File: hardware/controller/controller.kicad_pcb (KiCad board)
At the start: 4 copper layers, 59 x 47 mm, 55 parts, among them J1 Conn_01x02_Pin, J11 Barrel_Jack, J12 USB_C_Receptacle_USB2.0_14P, J2 Conn_01x02_Pin, J3 Conn_01x02_Pin, J5 Screw_Terminal_01x02, J6 Screw_Terminal_01x02, J7 Conn_01x04_Pin, J8 Conn_01x04_Pin, U1 ESP32-C3-MINI-1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

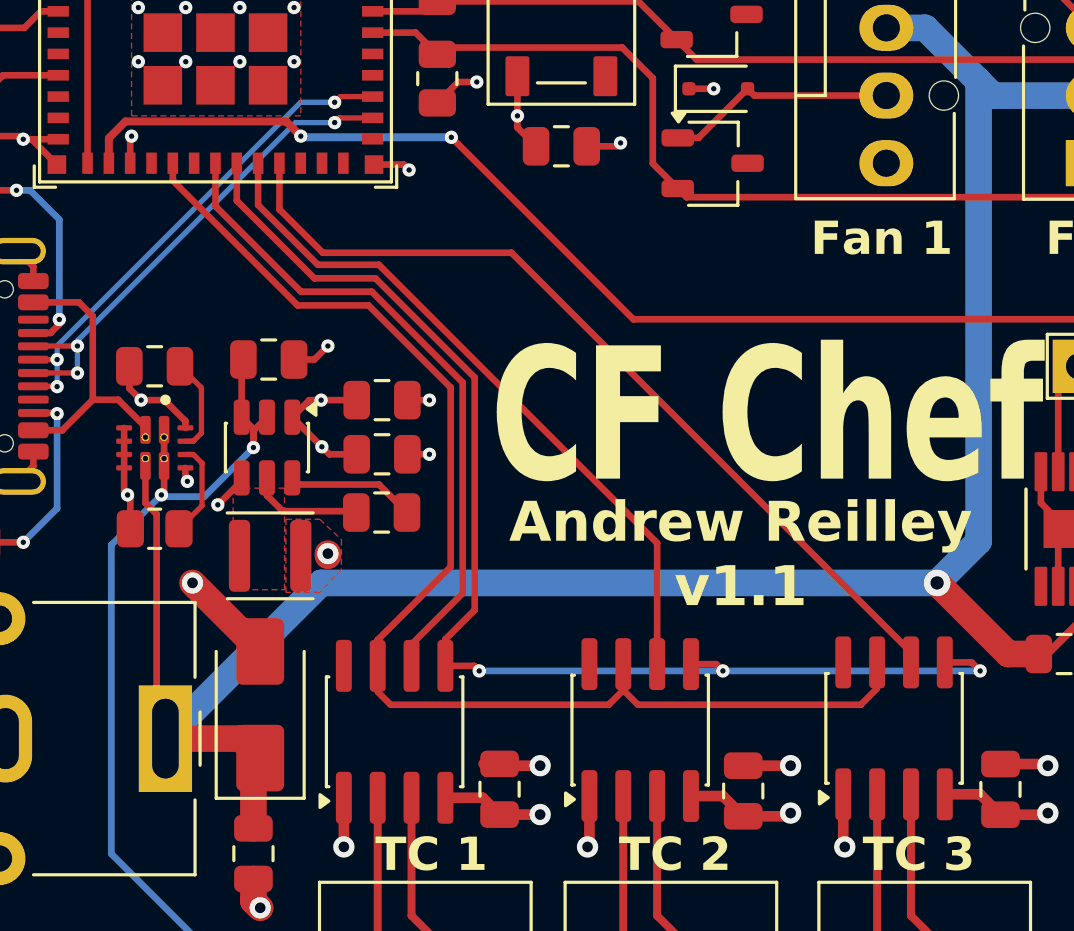
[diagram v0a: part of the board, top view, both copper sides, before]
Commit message: Reroute regulator
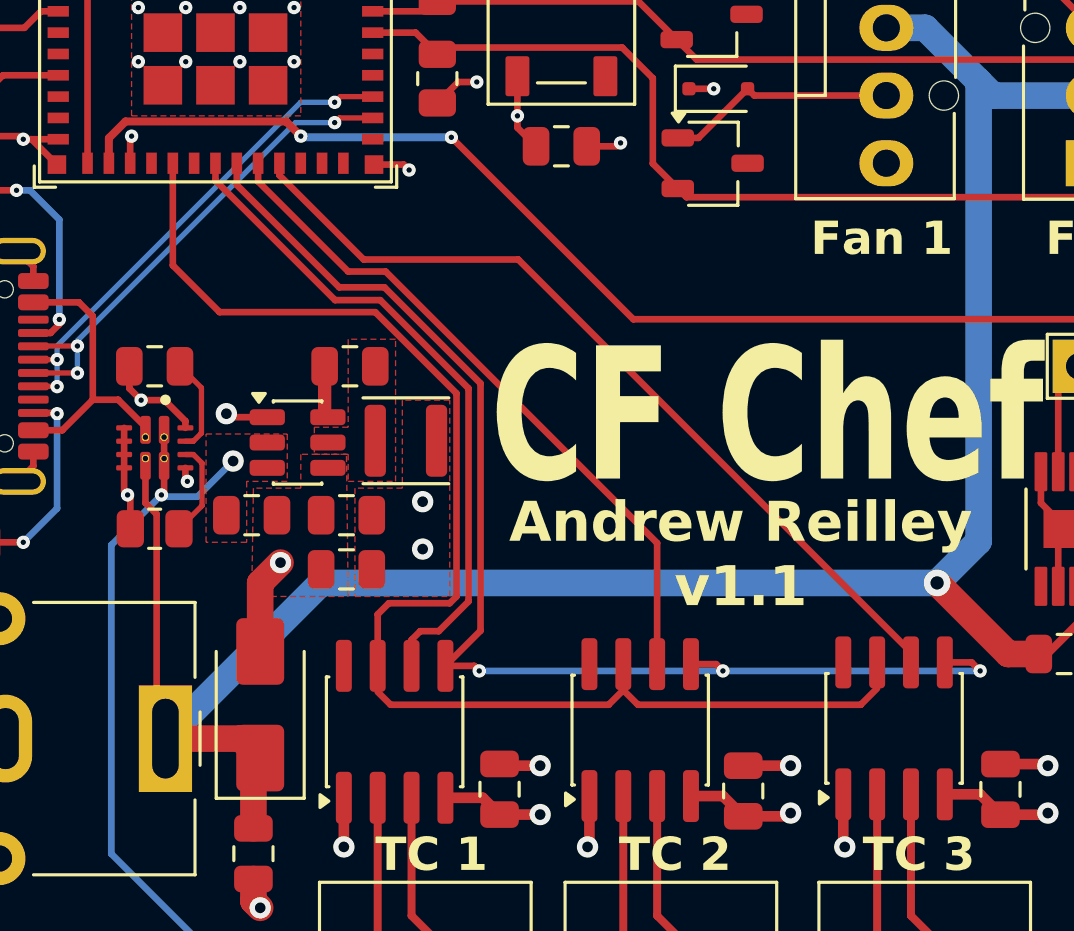
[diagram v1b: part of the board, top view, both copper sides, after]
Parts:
- moved L1 6.68 mm to (128.7, 93.0)
- moved C10 6.49 mm to (126.4, 97.8), turned to 180 degrees
- moved C11 5.88 mm to (122.9, 95.8)
- moved C13 5.61 mm to (126.6, 90.2), turned to 180 degrees
- moved C9 2.65 mm to (126.4, 95.8), turned to 180 degrees
- moved U8 1.16 mm to (124.6, 93.0), turned to 0 degrees
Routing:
- net VBUS: track 32.0 -> 26.2 mm
- net GND: track 78.7 -> 74.1 mm, vias 48 -> 44
- net Net-(U8-SW): track 4.28 -> 0.00 mm
- net +3V3: track 28.5 -> 24.3 mm
- net SO: track 45.5 -> 48.9 mm
- net Net-(U8-BST): track 4.84 -> 2.13 mm
- net CS2: track 32.7 -> 31.9 mm
- net CS1: track 26.3 -> 25.8 mm
- added copper zone on F.Cu, net VBUS

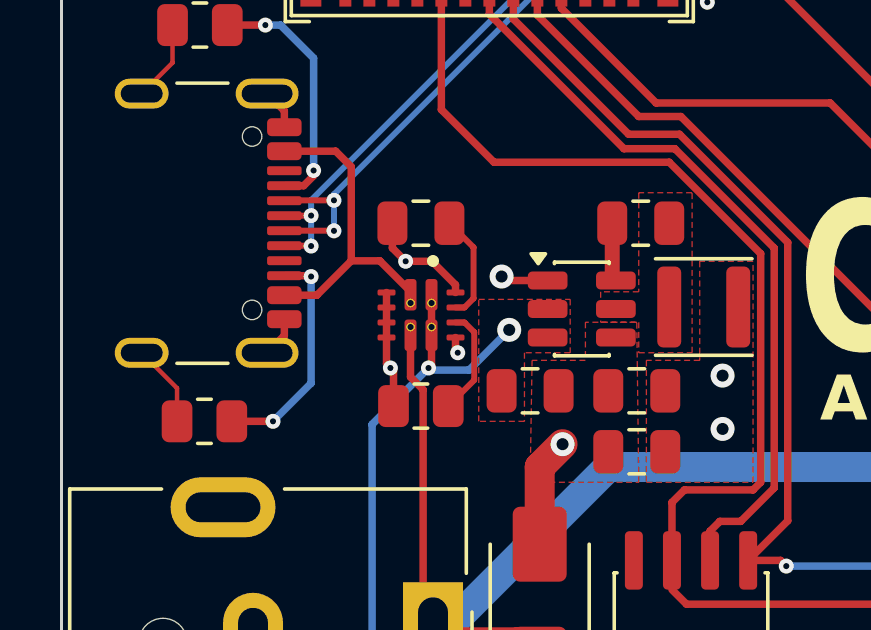
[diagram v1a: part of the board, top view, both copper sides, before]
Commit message: Increase via size for manufacturing
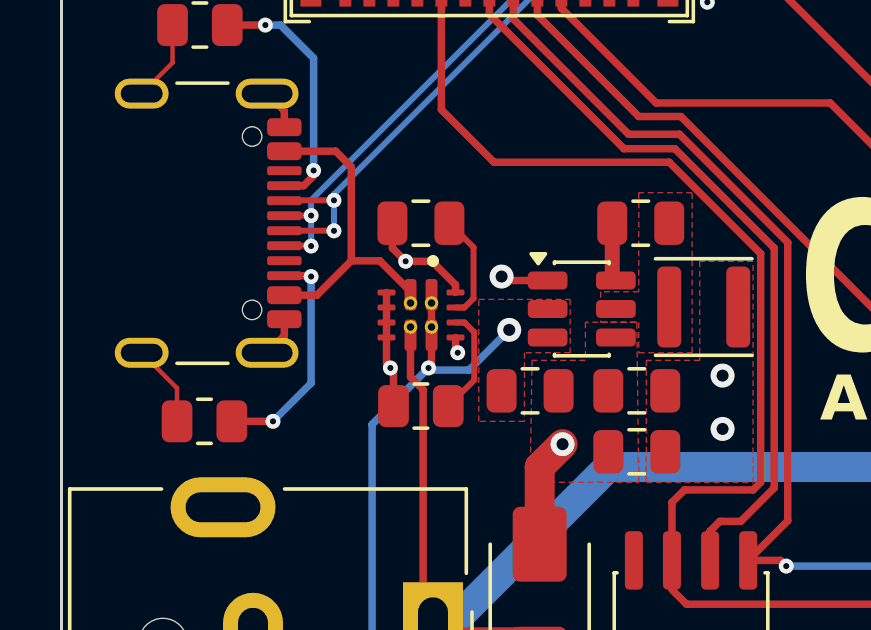
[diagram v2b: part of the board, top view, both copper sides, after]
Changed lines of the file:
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@@
 		(pad "1_1" thru_hole circle
 			(at -0.4 -0.35 270)
-			(size 0.3 0.3)
-			(drill 0.2)
+			(size 0.45 0.45)
+			(drill 0.25)
 			(layers "*.Cu")
 			(remove_unused_layers no)
@@
 		(pad "2_1" thru_hole circle
 			(at -0.4 0.35 270)
-			(size 0.3 0.3)
-			(drill 0.2)
+			(size 0.45 0.45)
+			(drill 0.25)
 			(layers "*.Cu")
 			(remove_unused_layers no)
@@
 		(pad "7_1" thru_hole circle
 			(at 0.4 0.35 270)
-			(size 0.3 0.3)
-			(drill 0.2)
+			(size 0.45 0.45)
+			(drill 0.25)
 			(layers "*.Cu")
 			(remove_unused_layers no)
@@
 		(pad "8_1" thru_hole circle
 			(at 0.4 -0.35 270)
-			(size 0.3 0.3)
-			(drill 0.2)
+			(size 0.45 0.45)
+			(drill 0.25)
 			(layers "*.Cu")
 			(remove_unused_layers no)
@@
 		(sheetname "/Microcontroller/")
 		(sheetfile "mcu.kicad_sch")
-		(attr exclude_from_pos_files)
+		(attr exclude_from_pos_files exclude_from_bom)
 		(fp_line
 			(start -1.2 -1.2)

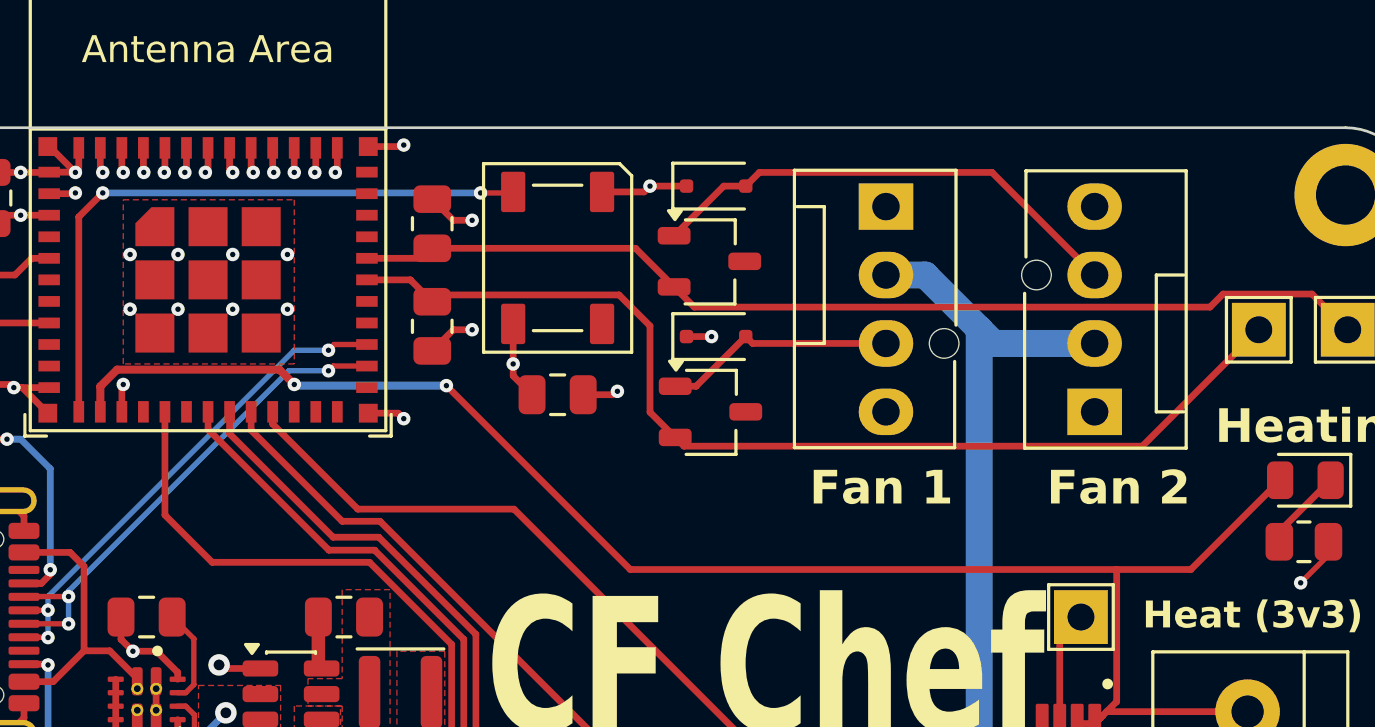
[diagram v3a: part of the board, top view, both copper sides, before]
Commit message: Fix diode footprints
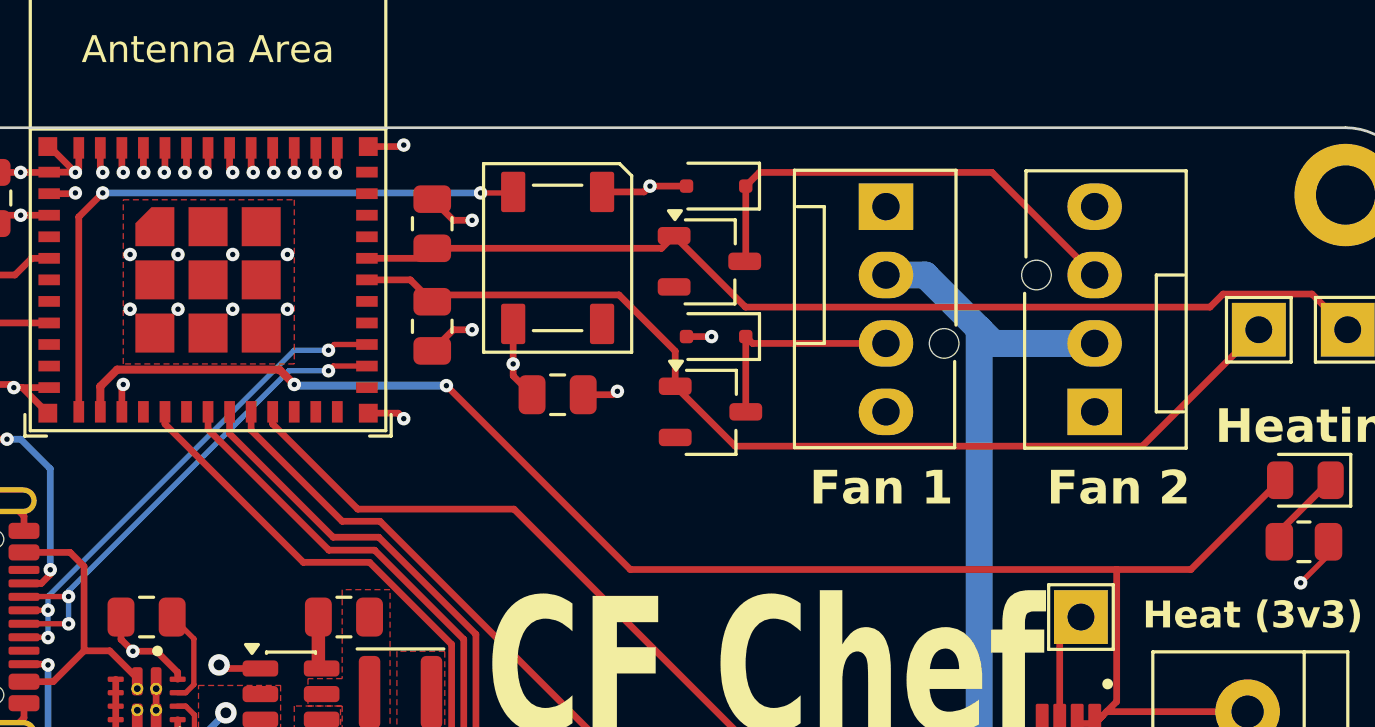
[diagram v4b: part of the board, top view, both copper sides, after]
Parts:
- turned D5 to 180 degrees
- turned D6 to 180 degrees
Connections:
- D3 pad 1: FAN_1_TACH -> Net-(D3-A)
- D3 pad 2: Net-(D3-A) -> (no net)
- D3 pad 3: (no net) -> FAN_1_TACH
- D4 pad 1: FAN_0_TACH -> Net-(D4-A)
- D4 pad 2: Net-(D4-A) -> (no net)
- D4 pad 3: (no net) -> FAN_0_TACH
- D5 pad 1: GND -> FAN_0_TACH
- D5 pad 2: FAN_0_TACH -> GND
- D6 pad 1: GND -> FAN_1_TACH
- D6 pad 2: FAN_1_TACH -> GND
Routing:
- net SO: track 48.9 -> 46.9 mm
- net Net-(D4-A): track 39.9 -> 38.8 mm
- net FAN_1_TACH: track 18.2 -> 17.6 mm
- net FAN_0_TACH: track 8.70 -> 8.11 mm

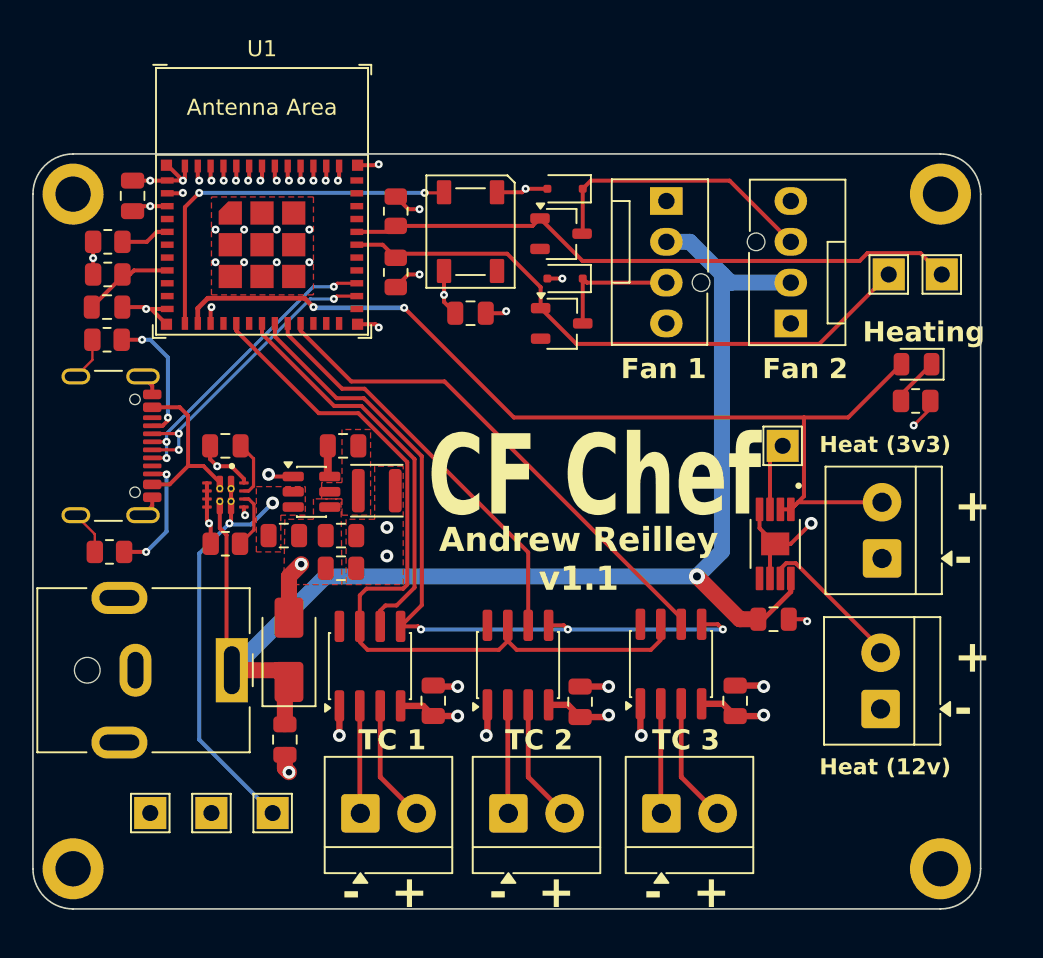
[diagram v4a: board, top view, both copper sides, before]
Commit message: Add filtering caps to thermocouples
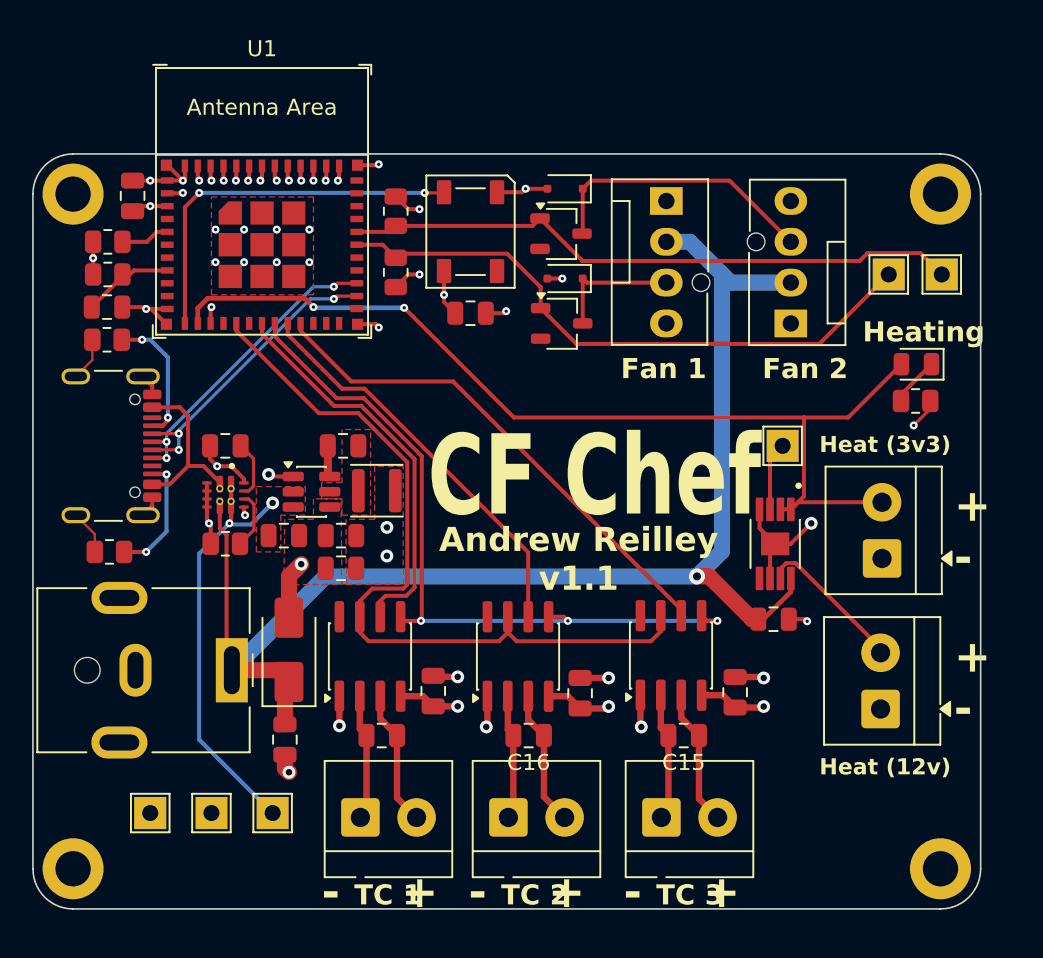
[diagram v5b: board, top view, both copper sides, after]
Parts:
- added C14: 10nF, Capacitor_SMD:C_0805_2012Metric, F.Cu at (129.0, 108.2)
- added C15: 10nF, Capacitor_SMD:C_0805_2012Metric, F.Cu at (147.8, 108.2)
- added C16: 10nF, Capacitor_SMD:C_0805_2012Metric, F.Cu at (138.1, 108.2)
- moved C4 0.60 mm to (132.2, 105.4)
- moved U2 0.60 mm to (128.2, 103.3)
- moved C3 0.53 mm to (151.0, 105.5)
- moved C6 0.53 mm to (141.3, 105.6)
- moved U3 0.53 mm to (137.4, 103.3)
- moved U4 0.53 mm to (147.0, 103.2)
- moved J1 0.25 mm to (127.6, 113.3)
- moved J2 0.25 mm to (136.8, 113.3)
- moved J3 0.25 mm to (146.4, 113.3)
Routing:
- net SCK: track 47.3 -> 45.6 mm
- net Net-(J1-Pin_1): track 7.60 -> 8.83 mm
- net SO: track 46.9 -> 48.1 mm
- net Net-(J2-Pin_1): track 7.67 -> 8.77 mm
- net Net-(J3-Pin_1): track 7.73 -> 8.68 mm
- net Net-(J1-Pin_2): track 7.63 -> 8.49 mm
- net Net-(J3-Pin_2): track 7.76 -> 8.55 mm
- net Net-(J2-Pin_2): track 7.70 -> 8.48 mm
- net CS1: track 25.8 -> 25.3 mm

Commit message: Add linear regulator for MAX chips
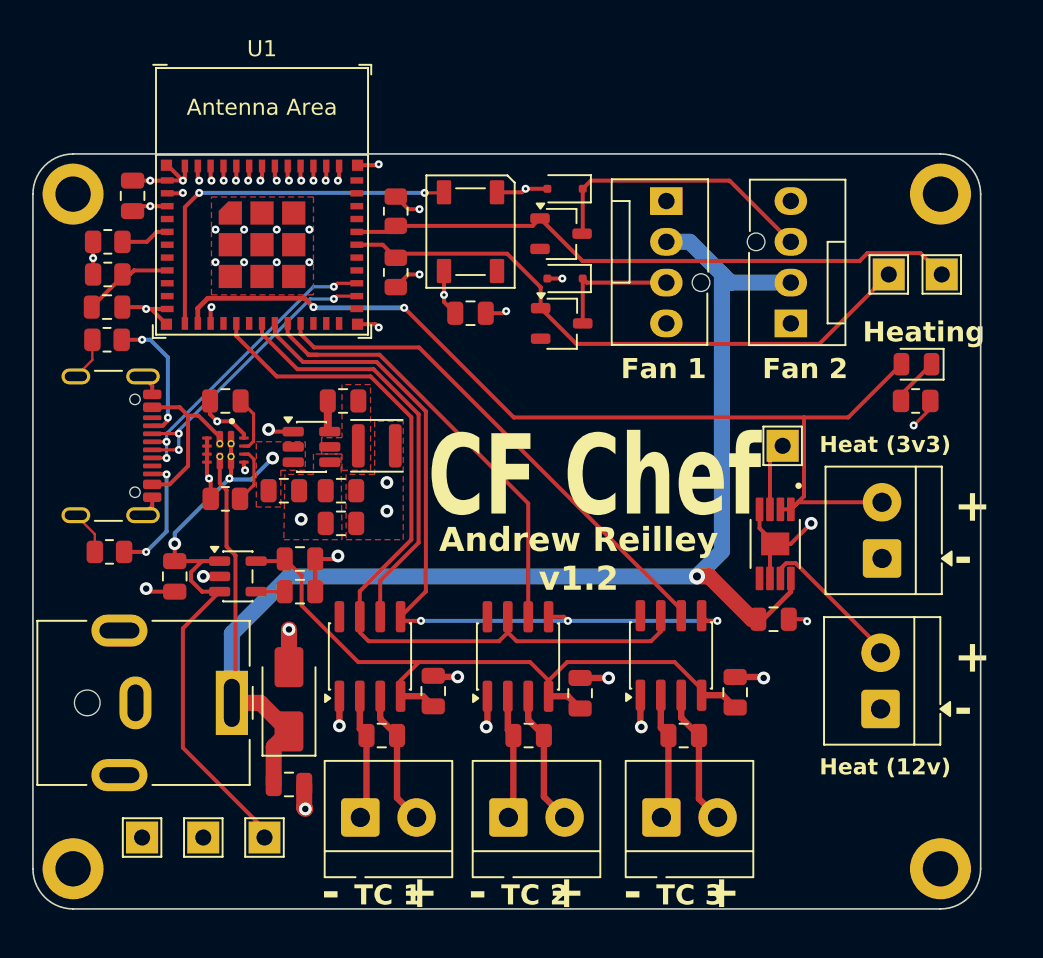
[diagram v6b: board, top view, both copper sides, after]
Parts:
- added C17: 1uF, Capacitor_SMD:C_0805_2012Metric, F.Cu at (116.1, 98.3)
- added C18: 10nF, Capacitor_SMD:C_0805_2012Metric, F.Cu at (123.9, 99.2)
- added C19: 2.2uF, Capacitor_SMD:C_0805_2012Metric, F.Cu at (123.9, 97.2)
- added U7: LP2985-3.3, Package_TO_SOT_SMD:SOT-23-5, F.Cu at (120.0, 98.3)
- moved D7 3.08 mm to (123.2, 106.0)
- moved C2 2.81 mm to (123.2, 111.3), turned to 0 degrees
- moved C10 2.79 mm to (126.4, 95.0)
- moved R12 2.79 mm to (119.2, 93.5)
- moved C11 2.79 mm to (122.9, 93.0)
- moved C13 2.79 mm to (126.6, 87.4)
- moved C5 2.79 mm to (119.2, 87.4)
- moved C9 2.79 mm to (126.4, 93.0)
- moved L1 2.79 mm to (128.7, 90.2)
- moved U5 2.79 mm to (119.2, 90.4)
- moved U8 2.79 mm to (124.6, 90.2)
- moved J11 2.03 mm to (119.6, 106.2)
- moved TP1 1.61 mm to (121.7, 114.6)
- moved TP2 1.61 mm to (117.9, 114.6)
- moved TP3 1.61 mm to (114.0, 114.6)
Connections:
- C3 pad 1: +3V3 -> +3.3VADC
- C4 pad 1: +3V3 -> +3.3VADC
- C6 pad 1: +3V3 -> +3.3VADC
- U2 pad 4: +3V3 -> +3.3VADC
- U3 pad 4: +3V3 -> +3.3VADC
- U4 pad 4: +3V3 -> +3.3VADC
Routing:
- net +3.3VADC: track 0.00 -> 44.1 mm
- net +3V3: track 24.3 -> 12.4 mm, vias 11 -> 8
- net VBUS: track 26.2 -> 37.8 mm, vias 2 -> 3
- net +12V: track 86.3 -> 94.7 mm
- net GND: track 74.1 -> 79.6 mm, vias 44 -> 48
- net CS1: track 25.3 -> 27.6 mm
- net SCK: track 45.6 -> 47.8 mm
- net Net-(U7-BP): track 0.00 -> 1.78 mm
- net CS0: track 24.8 -> 26.1 mm
- net SO: track 48.1 -> 49.2 mm
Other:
- board text added: "Andrew Reilley v1.2"
- board text removed: "Andrew Reilley v1.1"
